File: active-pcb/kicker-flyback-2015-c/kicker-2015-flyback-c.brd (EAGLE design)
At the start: 65.4 x 110.5 mm, 69 parts, among them J1 POWER, J2 CHIP, J3 KICK, J4 0528520870, Q1 STB40NF20, Q3 FDV303N, Q4 FQT1N80, Q5 FQT1N80, T1 DA2034, U1 LT3757, U2 IX4427N, U3 ATTINY441/841SSU/SSUR

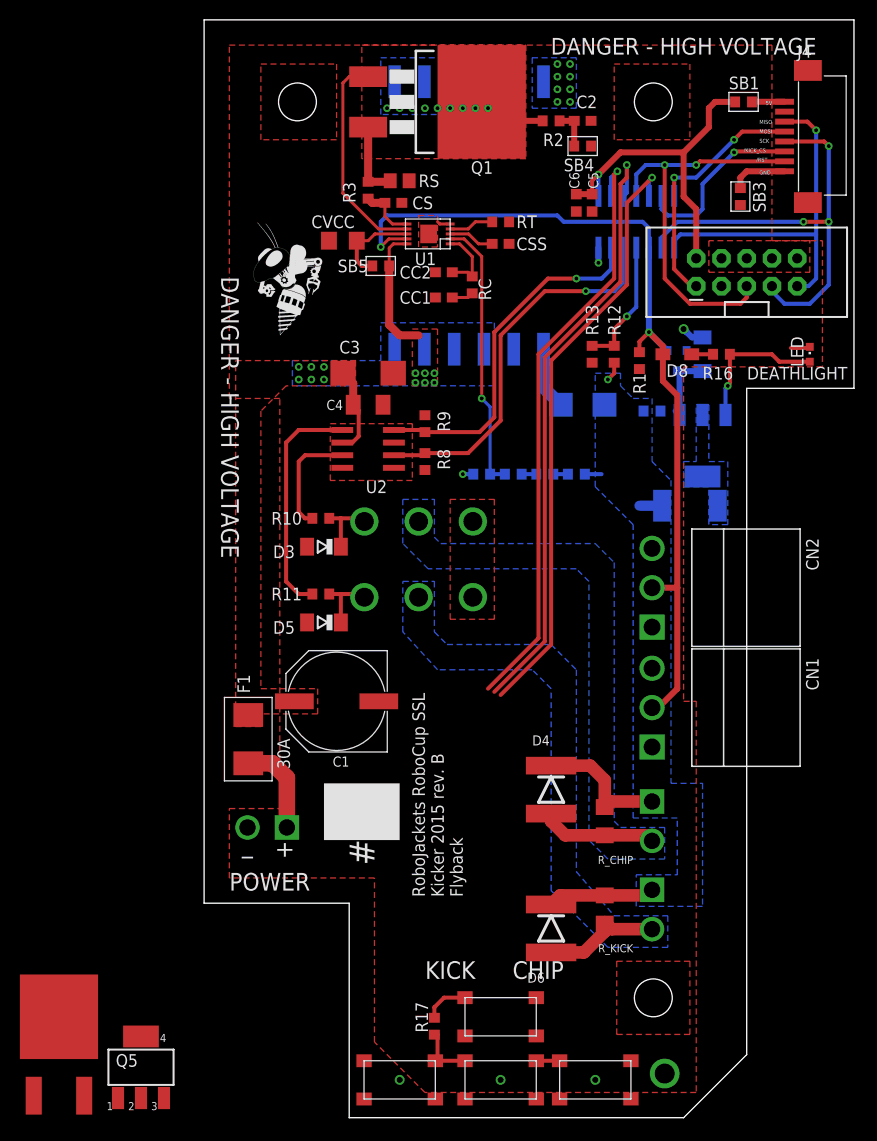
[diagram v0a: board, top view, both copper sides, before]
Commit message: Capacitor board version 3, final kicker prototype.
Capacitor board changed to two wire connection. Discharge circuit
upgraded on main board to give 8s discharge (down from 3 minutes).
Separate discharge circuit not needed for this reason. Wiring on main
board completed.
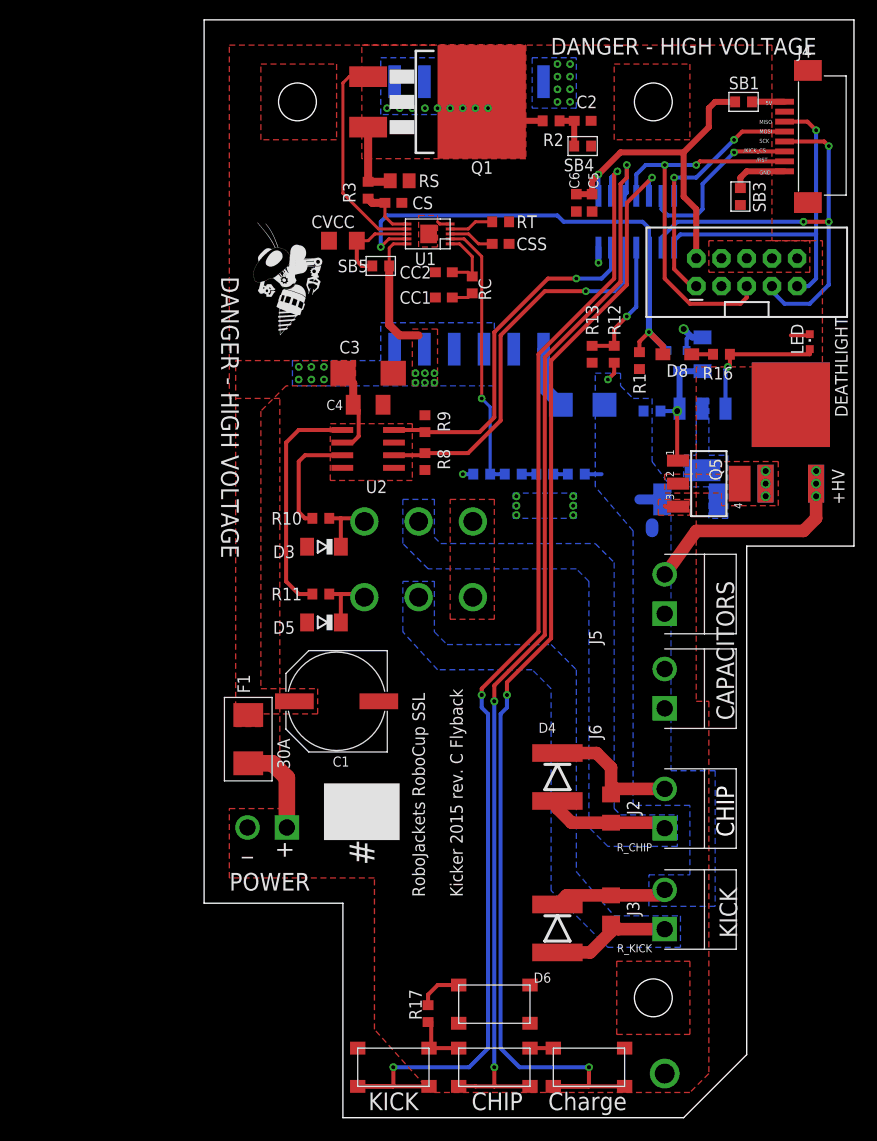
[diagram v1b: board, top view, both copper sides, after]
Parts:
- removed CN1, CN2: (no value), jst-vh:B3PS-VH
- added J5: Cap 1, jst_vh:JST_VH_2_RA
- added J6: Cap 2, jst_vh:JST_VH_2_RA
- added R19: PWR163S-25-3301J, RoboJackets-Resistors:PWR163S-25-3301J
- moved R18 96.0 mm to (59.1, 71.8)
- moved Q5 82.0 mm to (50.8, 63.8), turned to 270 degrees
- moved J2 1.80 mm to (46.4, 31.1), flipped to the top, turned to 90 degrees
- moved R_CHIP 1.42 mm to (41.0, 31.1)
- moved U$3 1.42 mm to (29.2, 5.08)
- moved U$4 1.42 mm to (38.7, 5.08)
- moved U$5 1.42 mm to (19.1, 5.08)
- moved R17 1.42 mm to (22.5, 10.5)
- moved U$2 1.42 mm to (29.2, 11.4)
- moved D4 1.42 mm to (35.6, 34.3)
- moved LED 1.27 mm to (61.0, 78.1)
- moved J3 1.27 mm to (46.4, 21.0), flipped to the top, turned to 90 degrees
- moved D6 0.64 mm to (35.6, 19.1)
- moved Q4 0.64 mm to (50.2, 68.3)
- moved R_KICK 0.64 mm to (41.0, 21.0)
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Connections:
- net +12V: now also C3.+, C4.1, U2.6
- net CHARGE: no longer CN1.2, CN2.2
- net GND: now also J5.1, J6.1; no longer CN1.3, CN2.3
- net HV: now also J2.2, J3.2, J5.2, J6.2, R19.P$2; no longer CN1.1, CN2.1, J2.1, J3.1
- net N$10: now also J3.1; no longer J3.2
- net N$11: now also J2.1; no longer J2.2
- net N$20: now also Q5.4, R19.P$3
- net VDD: no longer C3.+, C4.1, U2.6
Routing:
- net DB_KICK: track 60.2 -> 119.9 mm, vias 1 -> 3
- net DB_CHG: track 60.4 -> 118.3 mm, vias 1 -> 3
- net DB_CHIP: track 61.8 -> 108.7 mm, vias 1 -> 3
- net CHARGE: track 91.7 -> 51.6 mm
- net HV: track 30.4 -> 55.3 mm, vias 1 -> 4
- net VDD: track 44.0 -> 35.1 mm
- net +12V: track 13.1 -> 22.0 mm
- net N$21: track 7.28 -> 13.6 mm, vias 0 -> 1
- net GND: track 8.24 -> 11.3 mm, vias 11 -> 17
- net N$20: track 0.00 -> 1.27 mm, vias 0 -> 3
- net N$10: track 12.3 -> 12.9 mm
- added copper zone on layer 1, net N$20
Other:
- outline, holes or cut-outs redrawn
- board text added: "+HV"
- board text added: "CAPACITORS"
- board text added: "Charge"
- board text added: "Kicker 2015 rev. C Flyback"
- board text removed: "Kicker 2015 rev. B Flyback"

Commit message: Added board images
Added PNG files of the boards with dimensions and top layer labels.
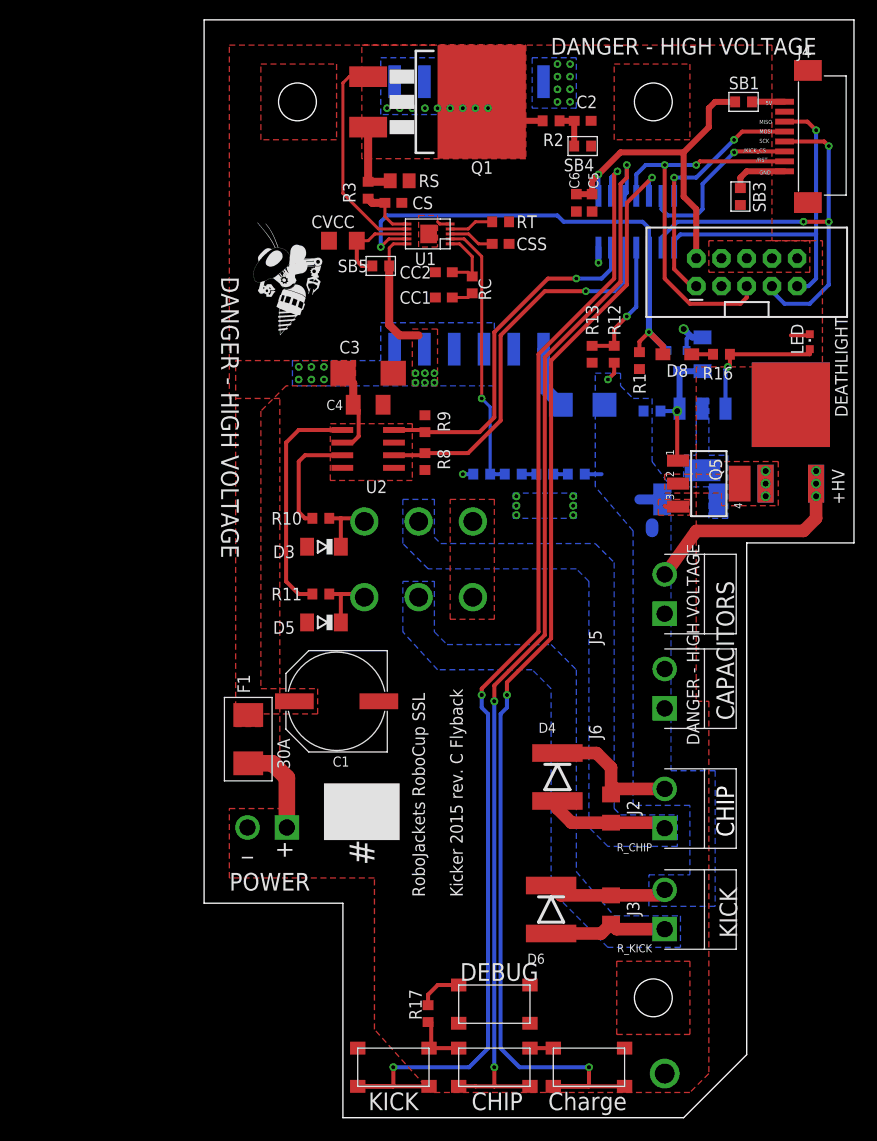
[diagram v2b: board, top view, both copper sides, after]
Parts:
- moved D6 2.01 mm to (34.9, 21.0)
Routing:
- net N$10: track 12.9 -> 12.1 mm
- net HV: track 55.3 -> 56.0 mm
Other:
- outline, holes or cut-outs redrawn
- board text added: "DEBUG"
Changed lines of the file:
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@@
 <plain>
 <wire x1="48.26" y1="0" x2="54.61" y2="6.35" width="0" layer="20"/>
-<wire x1="54.61" y1="6.35" x2="54.61" y2="57.531" width="0" layer="20"/>
-<wire x1="54.61" y1="57.531" x2="65.405" y2="57.531" width="0" layer="20"/>
-<wire x1="65.405" y1="57.531" x2="65.405" y2="110.49" width="0" layer="20"/>
+<wire x1="54.61" y1="6.35" x2="54.61" y2="57.8485" width="0" layer="20"/>
+<wire x1="54.61" y1="57.8485" x2="65.405" y2="57.8485" width="0" layer="20"/>
+<wire x1="65.405" y1="57.8485" x2="65.405" y2="110.49" width="0" layer="20"/>
 <wire x1="65.405" y1="110.49" x2="0" y2="110.49" width="0" layer="20"/>
 <wire x1="0" y1="110.49" x2="0" y2="21.59" width="0" layer="20"/>
@@
 <rectangle x1="8.5725" y1="25.7175" x2="34.6075" y2="44.7675" layer="22" rot="R90"/>
 <text x="3.4925" y="70.485" size="1.778" layer="21" ratio="15" rot="SR270" align="top-center">DANGER - HIGH VOLTAGE</text>
-<text x="46.99" y="106.9975" size="1.6764" layer="22" ratio="15" rot="SMR180" align="top-center">DANGER - HIGH VOLTAGE</text>
+<text x="48.26" y="108.585" size="1.6764" layer="22" ratio="15" rot="SMR0" align="top-center">DANGER - HIGH VOLTAGE</text>
 <text x="3.4925" y="70.485" size="1.778" layer="22" ratio="15" rot="SMR90" align="top-center">DANGER - HIGH VOLTAGE</text>
 <text x="17.145" y="25.4" size="2.54" layer="21" rot="R90">#</text>
@@
 <text x="55.88" y="94.9325" size="0.4064" layer="21">GND</text>
 <text x="54.2925" y="97.155" size="0.4064" layer="21">/KICK_CS</text>
-<rectangle x1="42.037" y1="8.255" x2="49.657" y2="15.875" layer="39" rot="R90"/>
+<rectangle x1="41.402" y1="8.255" x2="49.022" y2="15.875" layer="39" rot="R90"/>
 <rectangle x1="41.402" y1="8.255" x2="49.022" y2="15.875" layer="40" rot="R90"/>
 <text x="55.5625" y="96.2025" size="0.4064" layer="21">/RST</text>
-<text x="60.0075" y="40.005" size="1.27" layer="22" ratio="15" rot="SMR270" align="top-center">DANGER - HIGH VOLTAGE</text>
+<text x="48.5775" y="47.625" size="1.27" layer="22" ratio="15" rot="SMR270" align="top-center">DANGER - HIGH VOLTAGE</text>
 <text x="63.1825" y="63.5" size="1.27" layer="21" ratio="15" rot="SR90" align="top-center">+HV</text>
 <text x="53.34" y="40.005" size="1.778" layer="21" rot="R90">CAPACITORS</text>
@@
 <text x="32.0675" y="2.54" size="1.778" layer="21" rot="R180">CHIP</text>
 <text x="42.545" y="2.54" size="1.778" layer="21" rot="R180">Charge</text>
+<text x="33.655" y="15.5575" size="1.778" layer="21" rot="R180">DEBUG</text>
+<wire x1="13.97" y1="0" x2="13.97" y2="21.59" width="0.254" layer="47"/>
+<wire x1="13.97" y1="21.59" x2="0" y2="21.59" width="0.254" layer="47"/>
+<wire x1="0" y1="21.59" x2="0" y2="110.49" width="0.254" layer="47"/>
+<wire x1="0" y1="110.49" x2="65.405" y2="110.49" width="0.254" layer="47"/>
+<wire x1="65.405" y1="110.49" x2="65.405" y2="57.785" width="0.254" layer="47"/>
+<wire x1="65.405" y1="57.785" x2="54.61" y2="57.785" width="0.254" layer="47"/>
+<wire x1="54.61" y1="57.785" x2="54.61" y2="6.35" width="0.254" layer="47"/>
+<wire x1="54.61" y1="6.35" x2="48.26" y2="0" width="0.254" layer="47"/>
+<wire x1="48.26" y1="0" x2="13.97" y2="0" width="0.254" layer="47"/>
+<dimension x1="54.61" y1="6.35" x2="48.26" y2="0" x3="62.5475" y3="-7.9375" layer="47"/>
+<dimension x1="54.61" y1="57.785" x2="54.61" y2="6.35" x3="62.23" y3="32.0675" layer="47"/>
+<dimension x1="48.26" y1="0" x2="13.97" y2="0" x3="31.115" y3="-10.16" layer="47"/>
+<dimension x1="13.97" y1="0" x2="13.97" y2="21.59" x3="-7.62" y3="10.795" layer="47"/>
+<dimension x1="13.97" y1="21.59" x2="0" y2="21.59" x3="6.985" y3="-18.415" layer="47" dtype="vertical"/>
+<dimension x1="65.405" y1="57.785" x2="54.61" y2="57.785" x3="60.0075" y3="49.53" layer="47" dtype="vertical"/>
+<dimension x1="65.405" y1="110.49" x2="65.405" y2="57.785" x3="73.025" y3="84.1375" layer="47" dtype="vertical"/>
+<dimension x1="0" y1="110.49" x2="65.405" y2="110.49" x3="32.7025" y3="116.84" layer="47" dtype="vertical"/>
+<dimension x1="0" y1="21.59" x2="0" y2="110.49" x3="-7.62" y3="66.04" layer="47" dtype="vertical"/>
+<dimension x1="48.26" y1="0" x2="41.07579375" y2="0" x3="53.34" y3="5.08" layer="47" dtype="angle"/>
+<dimension x1="54.61" y1="6.35" x2="49.670859375" y2="1.41085625" x3="54.61" y3="13.335" layer="47" dtype="angle"/>
+<text x="48.5775" y="47.625" size="1.27" layer="21" ratio="15" rot="SR90" align="top-center">DANGER - HIGH VOLTAGE</text>
 </plain>
 <attributes>
@@
 </element>
 <element name="U2" library="RoboJackets-PowerICs" package="SOIC-8" value="IX4427N" x="16.51" y="67.31" rot="R90"/>
-<element name="D6" library="RoboJackets-Diodes" package="DO-214AB" value="" x="35.56" y="19.05" smashed="yes" rot="R270">
-<attribute name="NAME" x="34.925" y="14.605" size="1.016" layer="25" ratio="10" rot="R180"/>
-<attribute name="VALUE" x="31.115" y="22.86" size="1.016" layer="27" ratio="10" rot="R270"/>
+<element name="D6" library="RoboJackets-Diodes" package="DO-214AB" value="" x="34.925" y="20.955" smashed="yes" rot="R270">
+<attribute name="NAME" x="34.29" y="16.51" size="1.016" layer="25" ratio="10" rot="R180"/>
+<attribute name="VALUE" x="30.48" y="24.765" size="1.016" layer="27" ratio="10" rot="R270"/>
 </element>
 <element name="D4" library="RoboJackets-Diodes" package="DO-214AB" value="" x="35.56" y="34.29" smashed="yes" rot="R270">
@@
 <vertex x="39.37" y="63.5"/>
 </polygon>
-<wire x1="40.9575" y1="22.377" x2="36.474" y2="22.377" width="1.27" layer="1"/>
-<wire x1="36.474" y1="22.377" x2="35.56" y2="21.463" width="1.27" layer="1"/>
 <wire x1="45.797" y1="22.377" x2="40.9575" y2="22.377" width="1.27" layer="1"/>
 <contactref element="R18" pad="P$3"/>
@@
 <wire x1="49.53" y1="59.055" x2="46.355" y2="54.61" width="1.27" layer="1"/>
 <wire x1="46.355" y1="33.095" x2="41.5155" y2="33.095" width="1.27" layer="1"/>
+<wire x1="40.9575" y1="22.377" x2="35.916" y2="22.377" width="1.27" layer="1"/>
+<wire x1="35.916" y1="22.377" x2="34.925" y2="23.368" width="1.27" layer="1"/>
 <wire x1="46.355" y1="54.685" x2="46.355" y2="54.61" width="0" layer="19" extent="1-1"/>
 <wire x1="45.797" y1="22.377" x2="46.355" y2="22.935" width="0" layer="19" extent="1-1"/>
@@
 <contactref element="D6" pad="A"/>
 <contactref element="Q2" pad="C_BOT"/>
-<wire x1="35.56" y1="16.637" x2="38.862" y2="16.637" width="1.27" layer="1"/>
-<wire x1="38.862" y1="16.637" x2="40.9575" y2="18.7325" width="1.27" layer="1"/>
-<wire x1="40.9575" y1="19.533" x2="40.9575" y2="19.685" width="1.27" layer="1"/>
-<wire x1="40.9575" y1="19.533" x2="40.9575" y2="18.7325" width="1.27" layer="1"/>
-<wire x1="41.6675" y1="18.975" x2="40.9575" y2="19.685" width="1.27" layer="1"/>
 <polygon width="0.4064" layer="16" thermals="no">
 <vertex x="20.0025" y="53.975"/>
@@
 </polygon>
 <contactref element="J3" pad="1"/>
-<wire x1="46.355" y1="18.975" x2="41.6675" y2="18.975" width="1.27" layer="1"/>
+<wire x1="34.925" y1="18.542" x2="39.9665" y2="18.542" width="1.27" layer="1"/>
+<wire x1="39.9665" y1="18.542" x2="40.9575" y2="19.533" width="1.27" layer="1"/>
+<wire x1="46.355" y1="18.975" x2="41.5155" y2="18.975" width="1.27" layer="1"/>
+<wire x1="41.5155" y1="18.975" x2="40.9575" y2="19.533" width="1.27" layer="1"/>
 </signal>
 <signal name="N$7">

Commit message: Kicker Prototype 1
Added new igbt in parallel with old one, populate one at a time for
testing.
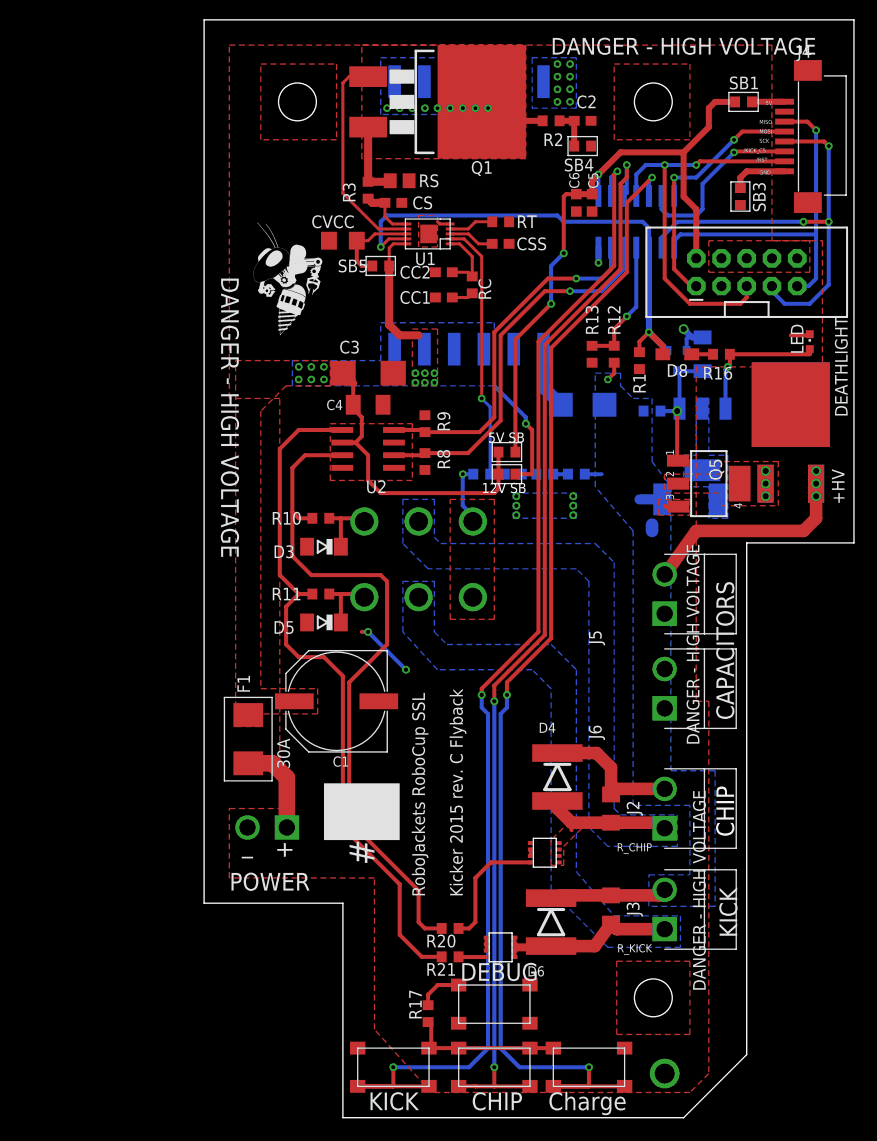
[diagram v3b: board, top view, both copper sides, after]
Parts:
- added R20, R21: 220, rcl:R0603
- added SB2: 5V_SEL, RoboJackets-Switches:SB0603
- added SB6: 12V Se, RoboJackets-Switches:SB0603
- added U$6, U$7: TIG058E8-TL-H, RoboJackets-IGBT:ECH8
- moved D6 1.27 mm to (34.9, 19.7)
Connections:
- new net GATE_C: R20.1, U$6.P4
- new net GATE_K: R21.1, U$7.P4
- new net N$15: C3.+, C4.1, SB2.1, SB6.1, U2.6
- net +12V: now also SB6.2; no longer C3.+, C4.1, U2.6
- net GND: now also U$6.P1, U$6.P2, U$6.P3, U$7.P1, U$7.P2, U$7.P3
- net N$10: now also U$7.P5, U$7.P6, U$7.P7, U$7.P8
- net N$11: now also U$6.P5, U$6.P6, U$6.P7, U$6.P8
- net N$16: now also R20.2
- net N$6: now also R21.2
- net VDD: now also SB2.2
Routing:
- net N$16: track 11.4 -> 68.6 mm
- net N$6: track 23.3 -> 70.0 mm
- net N$15: track 0.00 -> 31.2 mm
- net VDD: track 35.1 -> 64.2 mm, vias 1 -> 3
- net GND: track 11.3 -> 24.4 mm, vias 17 -> 19
- net GATE_C: track 0.00 -> 12.6 mm
- net N$17: track 8.50 -> 15.9 mm
- net N$10: track 12.1 -> 18.6 mm
- net +12V: track 22.0 -> 25.3 mm, vias 12 -> 13
- net GATE_K: track 0.00 -> 2.84 mm
- net N$11: track 11.6 -> 13.1 mm
- net CHIP: track 38.8 -> 38.1 mm
- added copper zone on layer 1, net N$11
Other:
- board text added: "12V SB"
- board text added: "5V SB"
